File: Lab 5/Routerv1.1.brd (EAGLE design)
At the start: 100 x 80 mm, 48 parts, among them J1 FTDI_DEVICERA_SMT, M1 WIRELESS-NRF24L01, U1 3.3V, U2 GY-521MPU6050

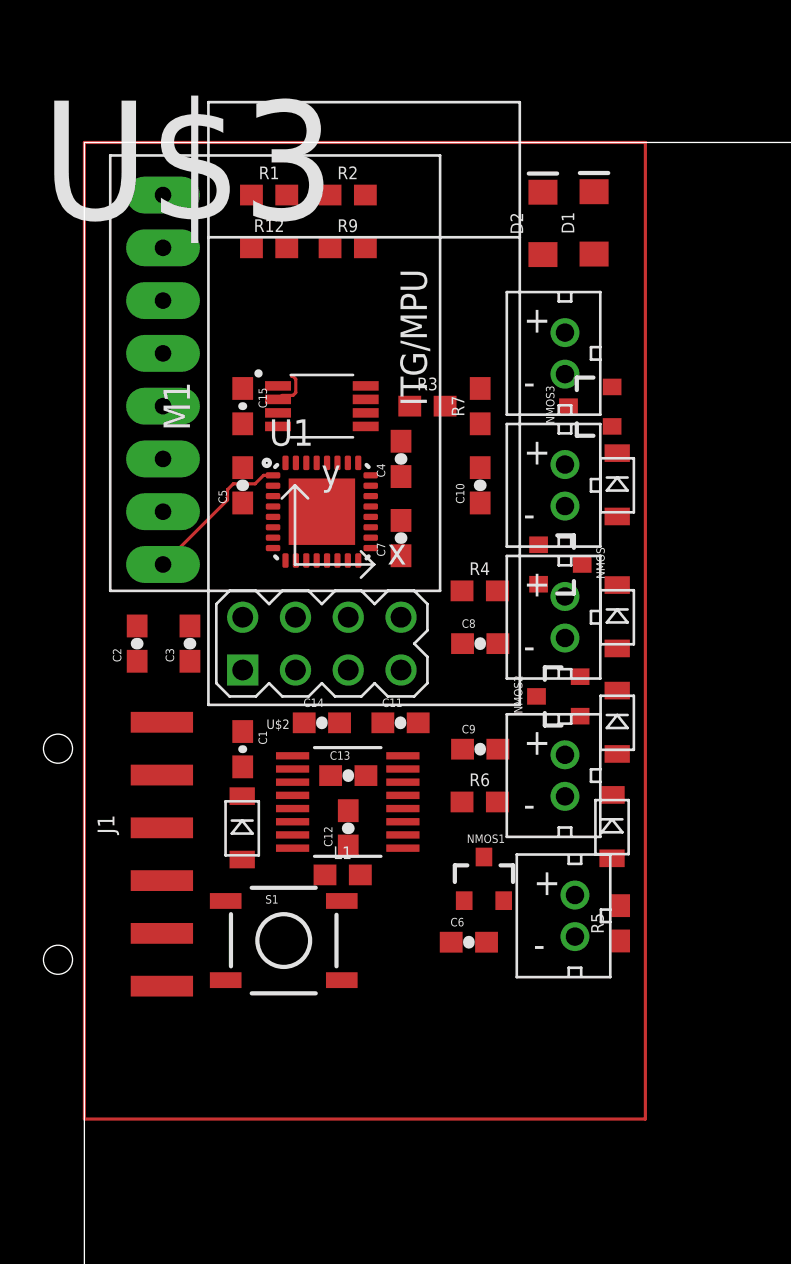
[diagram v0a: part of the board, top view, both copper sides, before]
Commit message: Check routev2.3.brd for one with no error
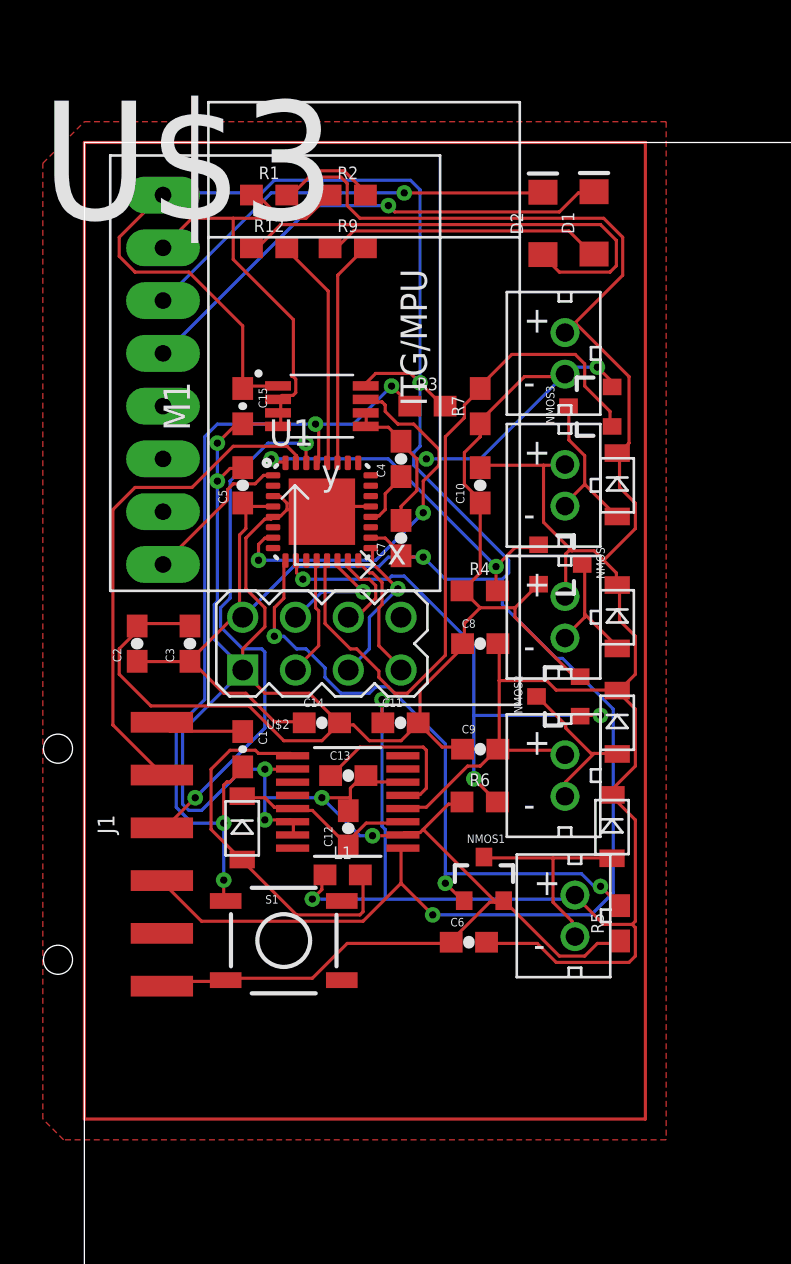
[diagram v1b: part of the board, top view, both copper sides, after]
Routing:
- net GND: track 1.90 -> 198.1 mm, vias 0 -> 8
- net VCC: track 0.00 -> 135.5 mm, vias 0 -> 3
- net BATTERY+: track 0.00 -> 132.0 mm, vias 0 -> 2
- net RESET: track 0.00 -> 41.3 mm, vias 0 -> 4
- net MOTOR4: track 0.00 -> 34.2 mm
- net MOTOR2: track 0.00 -> 31.7 mm, vias 0 -> 3
- net FTDI-RX: track 0.00 -> 25.9 mm, vias 0 -> 2
- net MOTOR3: track 0.00 -> 25.8 mm, vias 0 -> 3
- net FTDI-TX: track 0.00 -> 24.4 mm
- net IMU-SDA: track 0.00 -> 24.3 mm, vias 0 -> 1
- net N$9: track 0.00 -> 23.6 mm
- net IMU-SCL: track 0.00 -> 20.4 mm, vias 0 -> 1
- net OSC1: track 0.00 -> 18.6 mm, vias 0 -> 2
- net N$1: track 0.00 -> 18.2 mm
- net MOTOR1: track 0.00 -> 17.4 mm, vias 0 -> 2
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- added copper zone on layer 1, net GND
